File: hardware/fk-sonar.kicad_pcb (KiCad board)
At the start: 2 copper layers, 28.4 x 70.3 mm, 73 parts, among them J1 Conn_01x03, J2 CONN-HDR-2x5, J3 RF-SMA-EDGE, J4 MICRO-USB, J5 S2B-PH-SM4-TB, J6 Conn_01x04, J7 S2B-PH-SM4-TB, Q1 2N7002LT1G, Q2 2N7002LT1G, Q3 2N7002LT1G, Q4 2N7002LT1G, SW1 SPNO, U1 ATSAMD21G18A-AU, U2 RFM95W, U3 BQ24074RGTT, U4 S25FL116K0XMFI041, U5 MAX1704XX, U6 MCP1700T-3302E/MB, Y1 FC-135

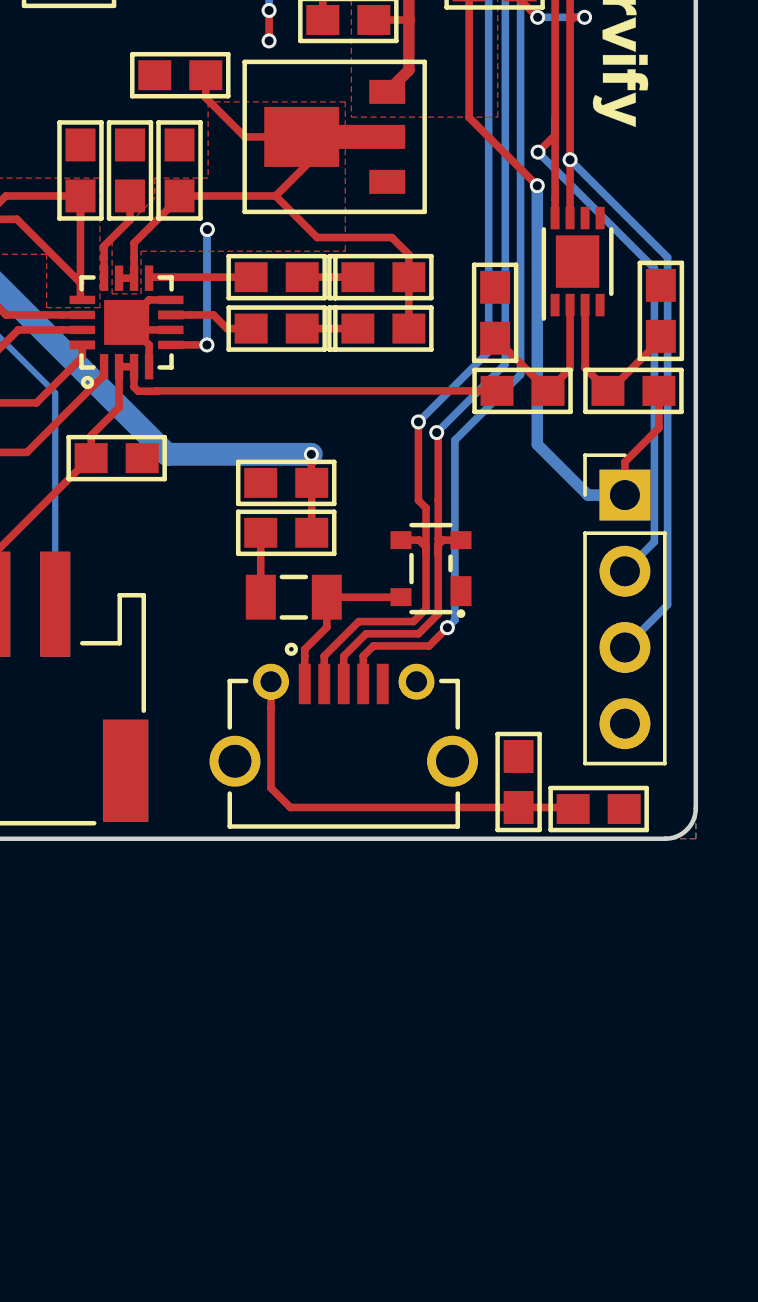
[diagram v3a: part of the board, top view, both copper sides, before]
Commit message: Labels on SDA/SCL header. Also made GND the square pad.
No room for the label there.
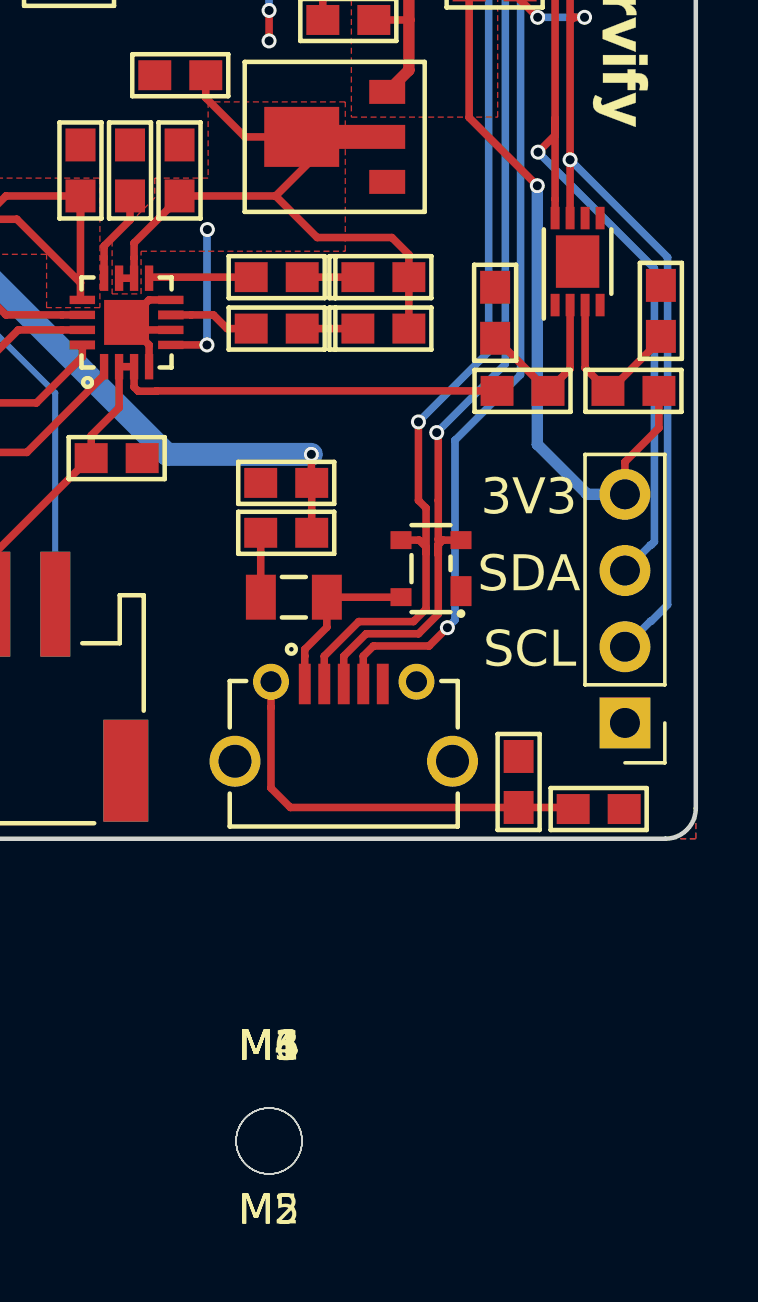
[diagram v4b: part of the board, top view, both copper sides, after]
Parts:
- added M1, M3, M4, M6: MOUNT_HOLE, RocketScreamKicadLibrary:HOLE_NPTH_2.2MM, F.Cu at (141.2, 187.0)
- added M2, M5: FIDUCIAL, RocketScreamKicadLibrary:FIDUCIAL-1MM, F.Cu at (141.2, 187.0)
- moved J6 7.59 mm to (153.1, 173.1), turned to 180 degrees
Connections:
- J6 pad 1: 3V3 -> GND
- J6 pad 2: /SDA -> /SCL
- J6 pad 3: /SCL -> /SDA
- J6 pad 4: GND -> 3V3
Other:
- board text added: "SCL"
- board text added: "SDA"

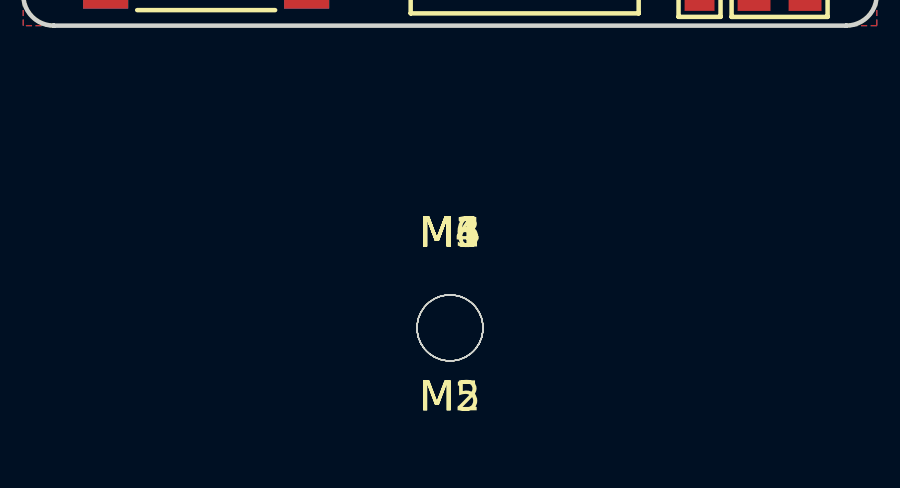
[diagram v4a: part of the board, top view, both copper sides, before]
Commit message: Easier fab label placements.
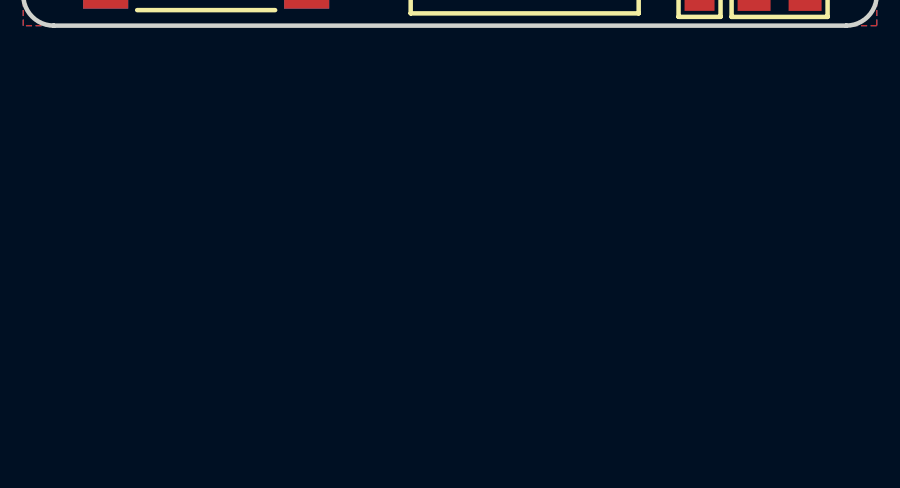
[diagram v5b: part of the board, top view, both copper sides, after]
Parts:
- removed M1, M3, M4, M6: MOUNT_HOLE, RocketScreamKicadLibrary:HOLE_NPTH_2.2MM
- removed M2, M5: FIDUCIAL, RocketScreamKicadLibrary:FIDUCIAL-1MM

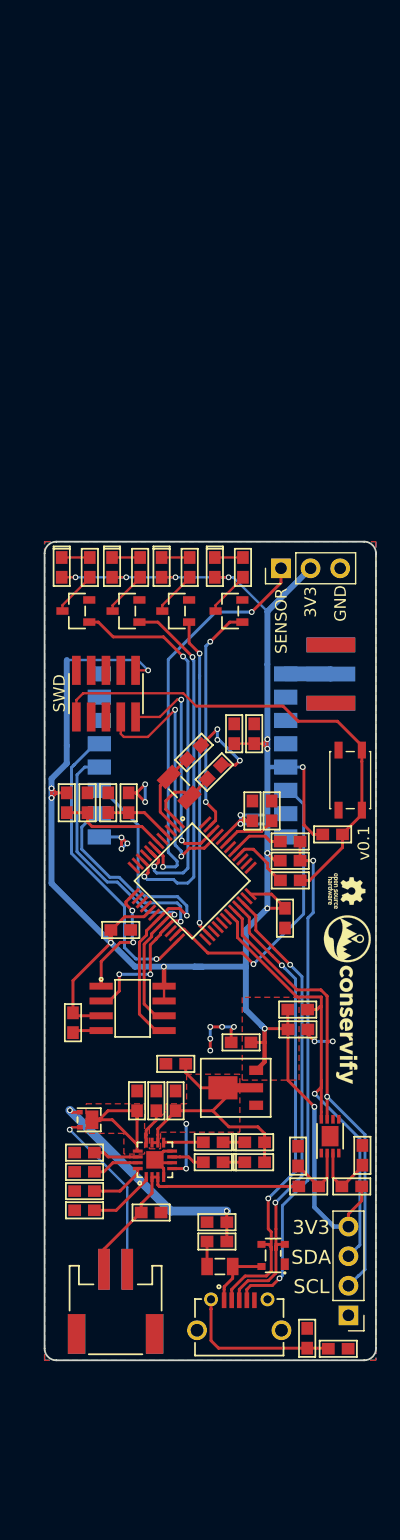
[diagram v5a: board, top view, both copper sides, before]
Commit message: Just some cleanup. Fix the fuel gauge lines.
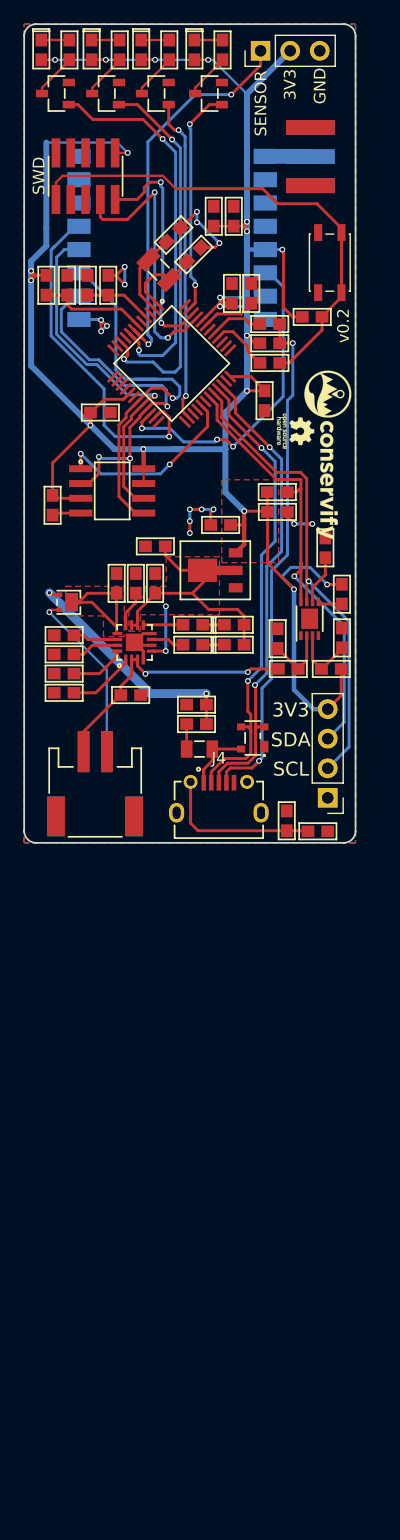
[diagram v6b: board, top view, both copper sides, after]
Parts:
- added R21: 4.7K, RocketScreamKicadLibrary:RES-0603, F.Cu at (152.5, 111.2)
- added R22: 4.7K, RocketScreamKicadLibrary:RES-0603, F.Cu at (151.1, 107.2)
- J4: footprint conservify:MICRO-USB -> RocketScreamKicadLibrary:MICRO-USB
- moved G*** 46.8 mm to (151.3, 99.2)
- moved J6 44.5 mm to (151.3, 128.7)
- moved C11 44.5 mm to (133.2, 110.3)
- moved C16 44.5 mm to (136.5, 110.3)
- moved C5 44.5 mm to (143.1, 85.4)
- moved C6 44.5 mm to (144.7, 85.4)
- moved C8 44.5 mm to (131.8, 95.6)
- moved D6 44.5 mm to (144.9, 123.5)
- moved D7 44.5 mm to (143.3, 115.5)
- moved Q2 44.5 mm to (132.2, 68.2)
- moved Q3 44.5 mm to (141.1, 68.2)
- moved Q4 44.5 mm to (136.5, 68.2)
- moved R10 44.5 mm to (128.7, 116.4)
- moved R16 44.5 mm to (139.7, 115.5)
- moved R3 44.5 mm to (146.3, 91.3)
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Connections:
- net /D3 renamed /SCL3
- net /SCL renamed /SCL1
- net /SDA renamed /SDA1
- J3 pad 2: Net-(J3-Pad2) -> GND
- U1 pad 13: /D4 -> /SDA3
- U1 pad 22: /ATN -> /RADIO_D0
- U1 pad 23: /D2 -> /RADIO_CS
- U1 pad 24: /D5 -> Net-(U1-Pad24)
- U1 pad 29: /D6 -> /FLASH_CS
- U2 pad 14: /D2 -> /RADIO_D0
- U2 pad 5: /D5 -> /RADIO_CS
- U4 pad 1: /D4 -> /FLASH_CS
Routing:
- net /RADIO_CS: track 0.00 -> 29.7 mm, vias 0 -> 1
- net /RADIO_D0: track 0.00 -> 27.7 mm, vias 0 -> 3
- net /D5: track 26.5 -> 0.00 mm, vias 1 -> 0
- net /D2: track 25.8 -> 0.00 mm, vias 1 -> 0
- net /FLASH_CS: track 0.00 -> 17.2 mm, vias 0 -> 2
- net /D4: track 10.8 -> 0.00 mm, vias 2 -> 0
- net 3V3: track 220.1 -> 227.7 mm, vias 18 -> 19
- net /MOSI: track 30.4 -> 34.7 mm
- net Net-(R22-Pad1): track 0.00 -> 4.24 mm
- net Net-(R21-Pad2): track 0.00 -> 2.10 mm
- net /A4: track 31.3 -> 32.9 mm
- net /MISO: track 27.8 -> 29.4 mm
- net /A2: track 33.6 -> 34.7 mm
- net /A1: track 34.9 -> 34.1 mm
- net VBAT: track 23.0 -> 23.3 mm, vias 0 -> 2
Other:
- net class Default: clearance 0.006 -> 0.1524; trace_width 0.006 -> 0.254
- rule trace_clearance: 0.006 -> 0.1524
- rule trace_min: 0.006 -> 0.19
- rule via_min_drill: 0.013 -> 0.3
- rule via_min_size: 0.027 -> 0.5
- board text added: "v0.2"
- board text removed: "v0.1"

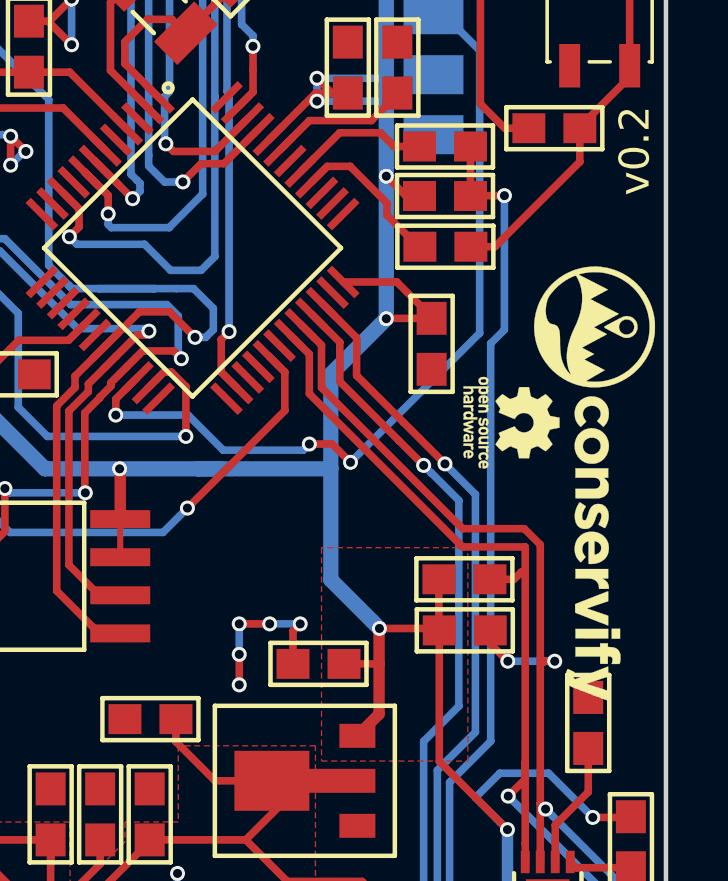
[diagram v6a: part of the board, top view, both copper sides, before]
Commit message: Exposing D30/D31 (as test points because stuff is kind of cramped)
If this becomes more regular/useful I'll make them pins or use a header.
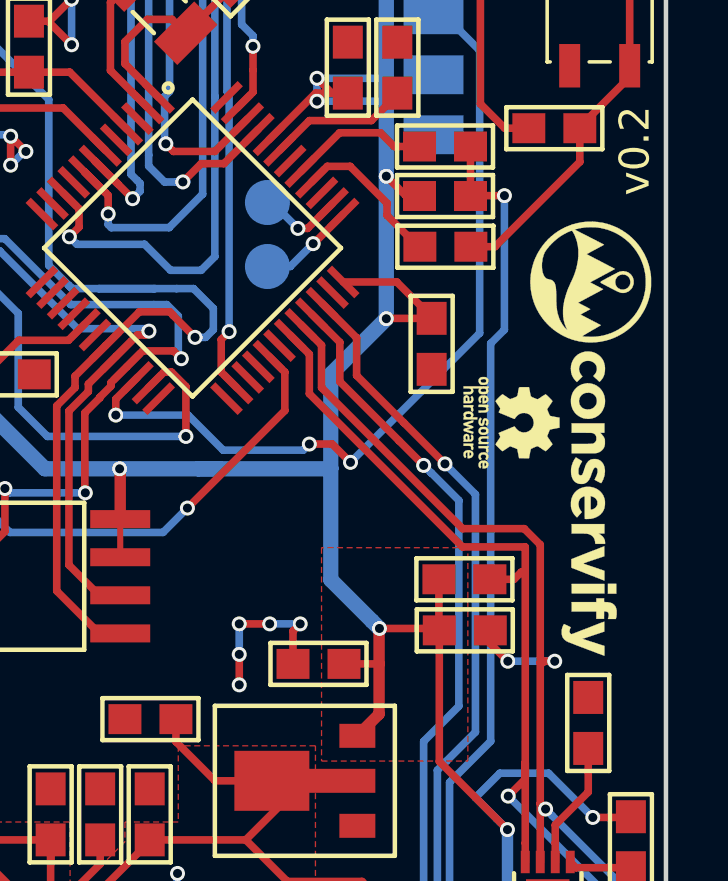
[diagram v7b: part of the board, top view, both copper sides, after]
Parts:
- added J8: Conn_01x01, Measurement_Points:Measurement_Point_Round-SMD-Pad_Small, B.Cu at (140.4, 89.9)
- added J9: Conn_01x01, Measurement_Points:Measurement_Point_Round-SMD-Pad_Small, B.Cu at (140.4, 92.0)
- moved G*** 1.50 mm to (151.2, 97.7)
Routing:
- net /D30: track 0.00 -> 3.25 mm, vias 0 -> 1
- net /D31: track 0.00 -> 2.87 mm, vias 0 -> 1
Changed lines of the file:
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@@
 (kicad_pcb (version 4) (host pcbnew 4.0.7-e2-6376~58~ubuntu16.04.1)
   (general
-    (links 186)
+    (links 188)
     (no_connects 0)
     (area 125.172399 62.180399 153.770401 132.612201)
     (thickness 1.6)
     (drawings 18)
-    (tracks 708)
+    (tracks 718)
     (zones 0)
-    (modules 75)
+    (modules 77)
     (nets 92)
   )
@@
   )
   (module conservify:conservify_text_negative_5000 (layer F.Cu)
-    (at 151.3078 99.2378 270)
+    (at 151.1808 97.7392 270)
     (fp_text reference G*** (at 0 0 270) (layer F.SilkS) hide
       (effects (font (thickness 0.3)))
@@
       (net 65 "Net-(J4-Pad9)"))
   )
+  (module Measurement_Points:Measurement_Point_Round-SMD-Pad_Small (layer B.Cu)
+    (at 140.4112 89.8652)
+    (descr "Mesurement Point, Round, SMD Pad, DM 1.5mm,")
+    (tags "Mesurement Point Round SMD Pad 1.5mm")
+    (attr virtual)
+    (fp_text reference J8 (at 0 2) (layer B.SilkS) hide
+      (effects (font (size 1 1) (thickness 0.15)) (justify mirror))
+    )
+    (fp_text value Conn_01x01 (at 0 -2) (layer B.Fab)
+      (effects (font (size 1 1) (thickness 0.15)) (justify mirror))
+    )
+    (fp_circle (center 0 0) (end 1 0) (layer B.CrtYd) (width 0.05))
+    (pad 1 smd circle (at 0 0) (size 1.5 1.5) (layers B.Cu B.Mask)
+      (net 27 /D31))
+  )
+  (module Measurement_Points:Measurement_Point_Round-SMD-Pad_Small (layer B.Cu)
+    (at 140.4112 91.9988)
+    (descr "Mesurement Point, Round, SMD Pad, DM 1.5mm,")
+    (tags "Mesurement Point Round SMD Pad 1.5mm")
+    (attr virtual)
+    (fp_text reference J9 (at 0 2) (layer B.SilkS) hide
+      (effects (font (size 1 1) (thickness 0.15)) (justify mirror))
+    )
+    (fp_text value Conn_01x01 (at 0 -2) (layer B.Fab)
+      (effects (font (size 1 1) (thickness 0.15)) (justify mirror))
+    )
+    (fp_circle (center 0 0) (end 1 0) (layer B.CrtYd) (width 0.05))
+    (pad 1 smd circle (at 0 0) (size 1.5 1.5) (layers B.Cu B.Mask)
+      (net 26 /D30))
+  )
   (gr_text SCL (at 148.1582 126.2126) (layer F.SilkS)
     (effects (font (size 1.2 1.2) (thickness 0.2)))
@@
   (segment (start 125.844278 84.2518) (end 125.844278 83.439) (width 0.508) (layer B.Cu) (net 2))
   (segment (start 125.844278 83.439) (end 125.844278 84.2518) (width 0.254) (layer F.Cu) (net 2))
-  (via (at 125.844278 84.2518) (size 0.5) (drill 0.3) (layers F.Cu B.Cu) (net 2) (status 1000000))
+  (via (at 125.844278 84.2518) (size 0.5) (drill 0.3) (layers F.Cu B.Cu) (net 2))
   (segment (start 125.844278 83.439) (end 125.844278 82.605666) (width 0.508) (layer B.Cu) (net 2))
   (segment (start 126.226178 83.8209) (end 125.844278 83.439) (width 0.254) (layer F.Cu) (net 2))
@@
   (segment (start 145.110211 122.737589) (end 145.110211 122.8598) (width 0.254) (layer F.Cu) (net 25))
   (segment (start 145.110211 122.555) (end 145.110211 121.259611) (width 0.254) (layer F.Cu) (net 25))
+  (segment (start 141.9352 91.2368) (end 141.950087 91.2368) (width 0.254) (layer F.Cu) (net 26))
+  (segment (start 141.950087 91.2368) (end 142.935858 90.251029) (width 0.254) (layer F.Cu) (net 26))
+  (segment (start 140.4112 91.9988) (end 141.1732 91.9988) (width 0.254) (layer B.Cu) (net 26))
+  (segment (start 141.1732 91.9988) (end 141.9352 91.2368) (width 0.254) (layer B.Cu) (net 26))
+  (via (at 141.9352 91.2368) (size 0.5) (drill 0.3) (layers F.Cu B.Cu) (net 26))
+  (segment (start 141.4272 90.7288) (end 141.750981 90.7288) (width 0.254) (layer F.Cu) (net 27))
+  (segment (start 141.750981 90.7288) (end 142.582305 89.897476) (width 0.254) (layer F.Cu) (net 27))
+  (segment (start 140.4112 89.8652) (end 140.5636 89.8652) (width 0.254) (layer B.Cu) (net 27))
+  (segment (start 140.5636 89.8652) (end 141.4272 90.7288) (width 0.254) (layer B.Cu) (net 27))
+  (via (at 141.4272 90.7288) (size 0.5) (drill 0.3) (layers F.Cu B.Cu) (net 27))
   (segment (start 145.4803 87.9983) (end 144.6332 87.9983) (width 0.254) (layer F.Cu) (net 29))
   (segment (start 144.6332 87.9983) (end 144.17601 87.54111) (width 0.254) (layer F.Cu) (net 29))
